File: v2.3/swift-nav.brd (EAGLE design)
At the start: 53 x 53 mm, 150 parts, among them J1 SMA_EDGE, J6 ZX62-B-5PA, Q1 IRLML6401, U1 6SLX9FTG256, U10 MAX2769, U12 PT7M8206B33TA5EX, U13 M25PX80, U2 LTC3407A_DFN, U3 STM32-M-64-LQFP, U4 7Q-16.368MBG-T, U5 SMA_PATCH_SMDGND, U6 93LC56BT-I/OT, U7 FT232HQ, U8 B4050, U9 XC2401, X3 FPGA DEBUG, X4 NX5032GA-12M, X5 CONN_5-2

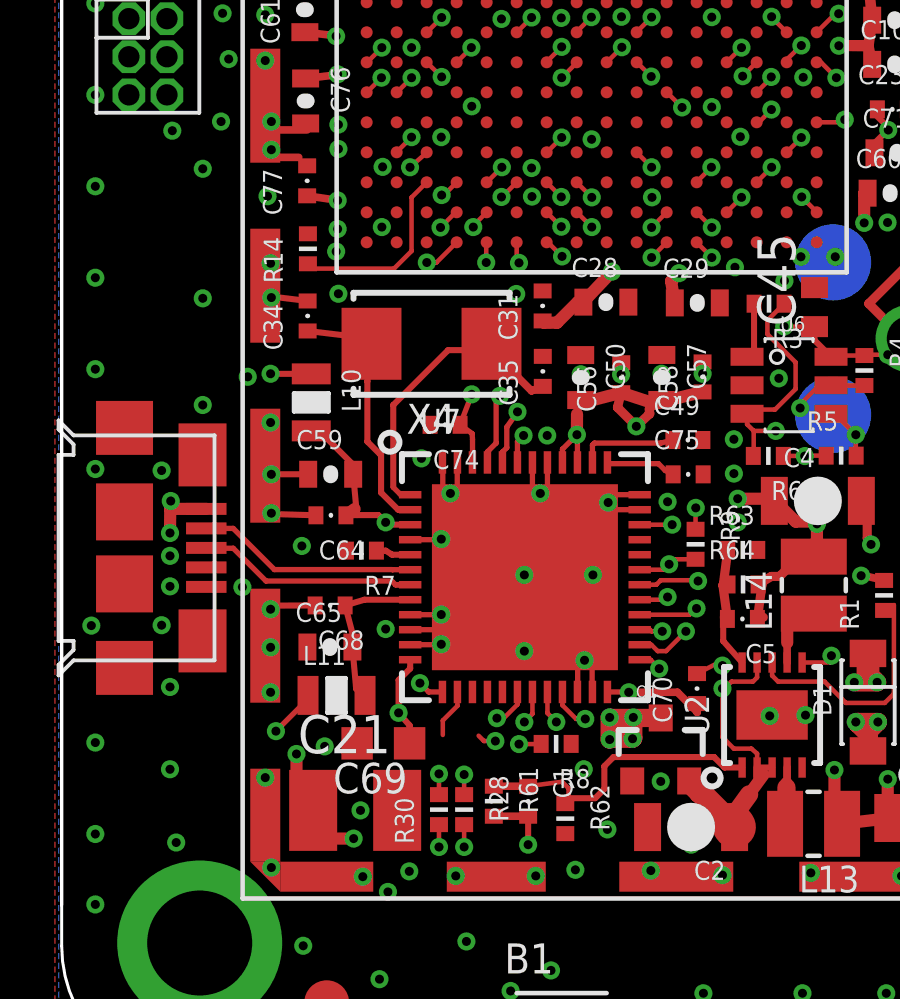
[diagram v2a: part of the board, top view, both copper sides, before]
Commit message: Routed some FTDI signals
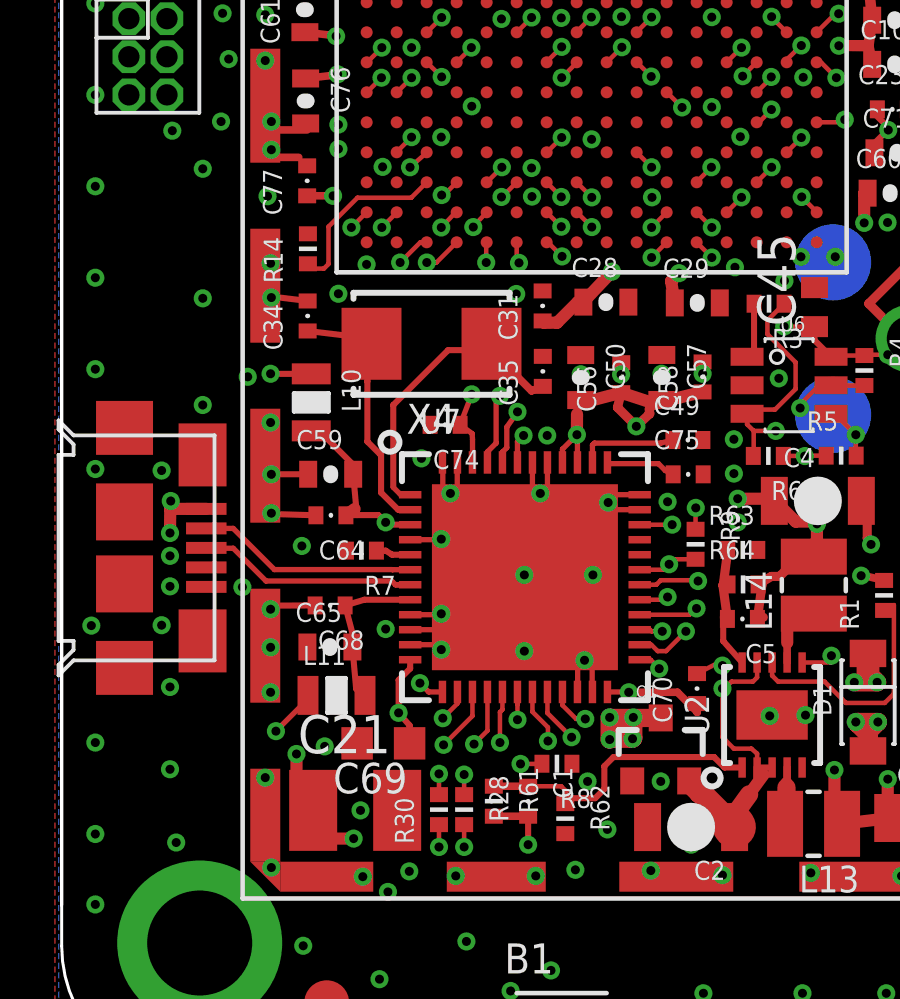
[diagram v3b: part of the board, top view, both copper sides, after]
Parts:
- moved R8 0.66 mm to (19.9, 14.0)
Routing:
- net FTDI_ADBUS2: track 0.00 -> 24.2 mm, vias 0 -> 2
- net FTDI_ADBUS3: track 0.00 -> 23.7 mm, vias 0 -> 2
- net FTDI_ADBUS4: track 0.00 -> 23.5 mm, vias 0 -> 2
- net UART6_TX/FTDI_ADBUS1: track 52.8 -> 50.7 mm
- net FTDI_ADBUS7: track 24.8 -> 26.8 mm
- net FTDI_ADBUS6: track 21.1 -> 22.8 mm
- net GND: vias 396 -> 394

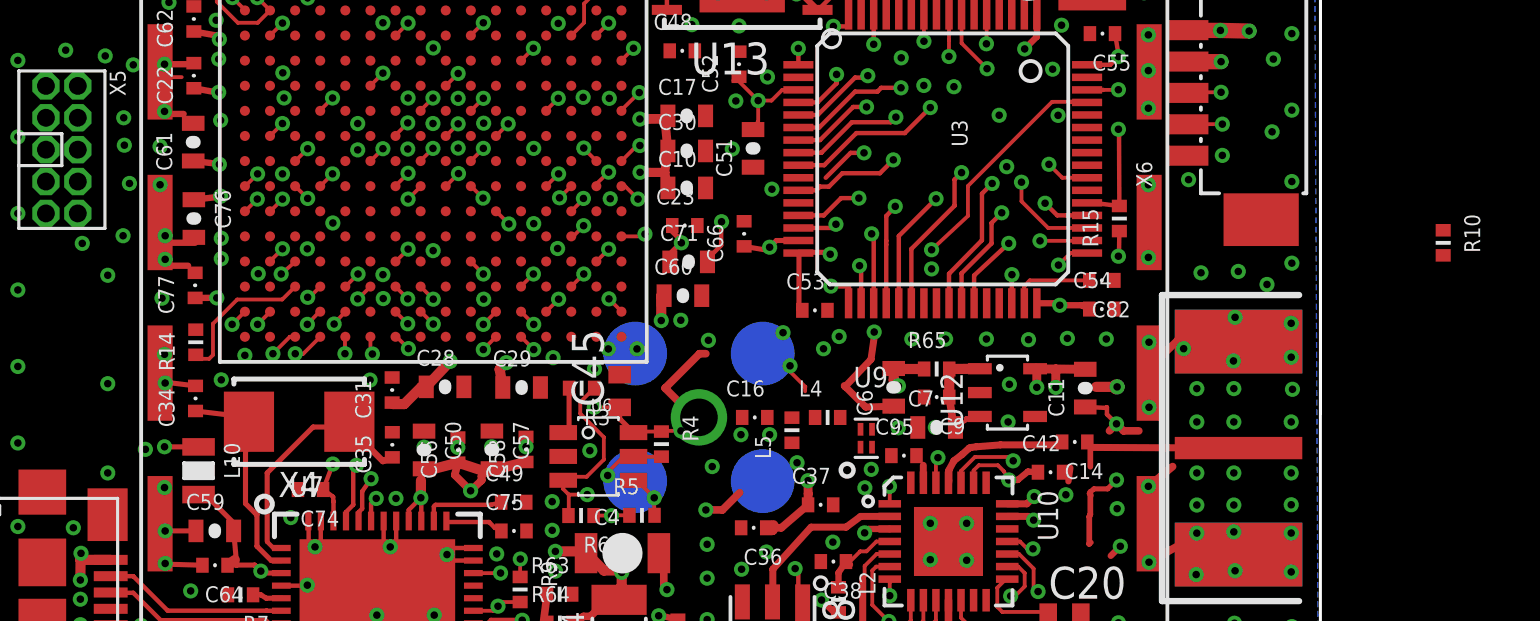
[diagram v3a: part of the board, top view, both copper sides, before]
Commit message: Routed rest of FTDI signals and added resistor to V_USB
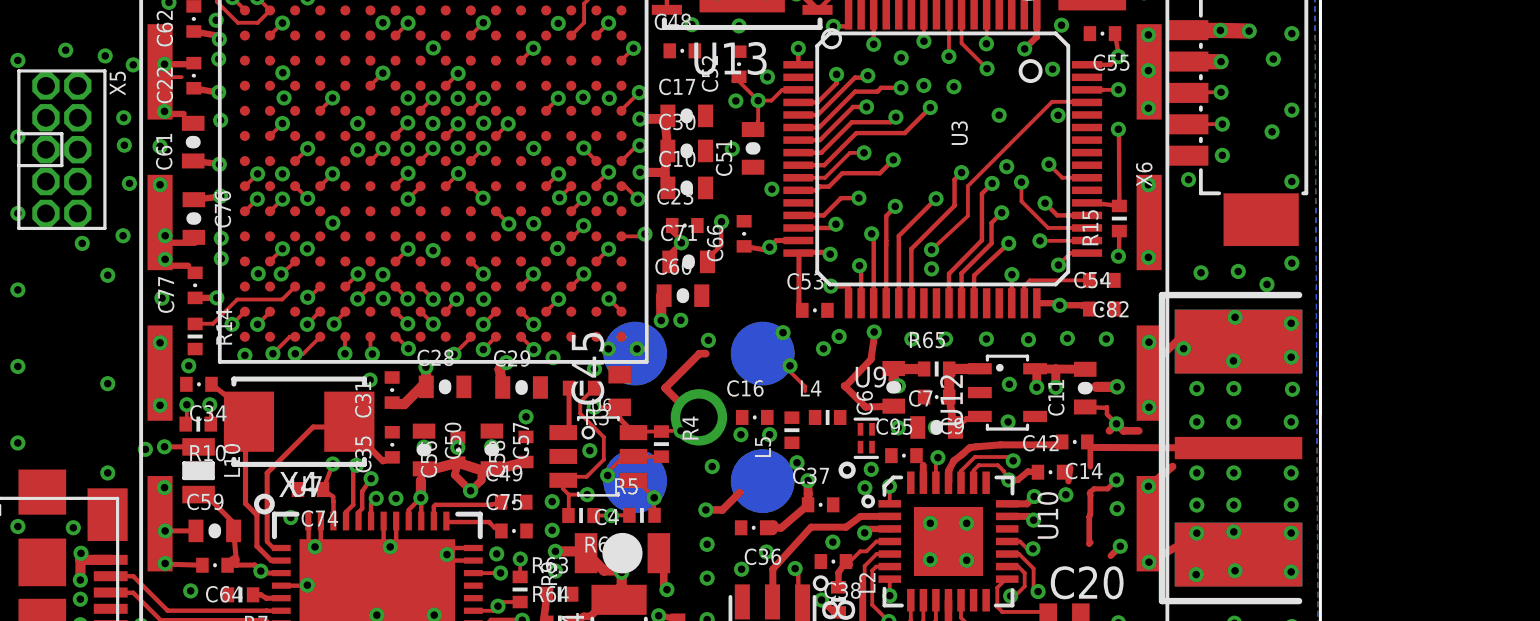
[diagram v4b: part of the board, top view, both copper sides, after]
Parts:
- moved R10 50.1 mm to (11.7, 27.9), turned to 180 degrees
- moved C34 0.58 mm to (11.7, 29.5), turned to 180 degrees
- moved R14 0.23 mm to (11.6, 31.4), turned to 270 degrees
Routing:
- net N$18: track 0.00 -> 68.0 mm, vias 0 -> 2
- net V_USB: track 131.8 -> 67.3 mm
- net UART6_TX/FTDI_ADBUS1: track 50.7 -> 52.3 mm, vias 2 -> 3
- net N$34: track 6.03 -> 4.60 mm
- net GND: track 82.6 -> 81.3 mm
- net UART6_RX/FTDI_ADBUS0: track 51.6 -> 52.7 mm, vias 2 -> 3

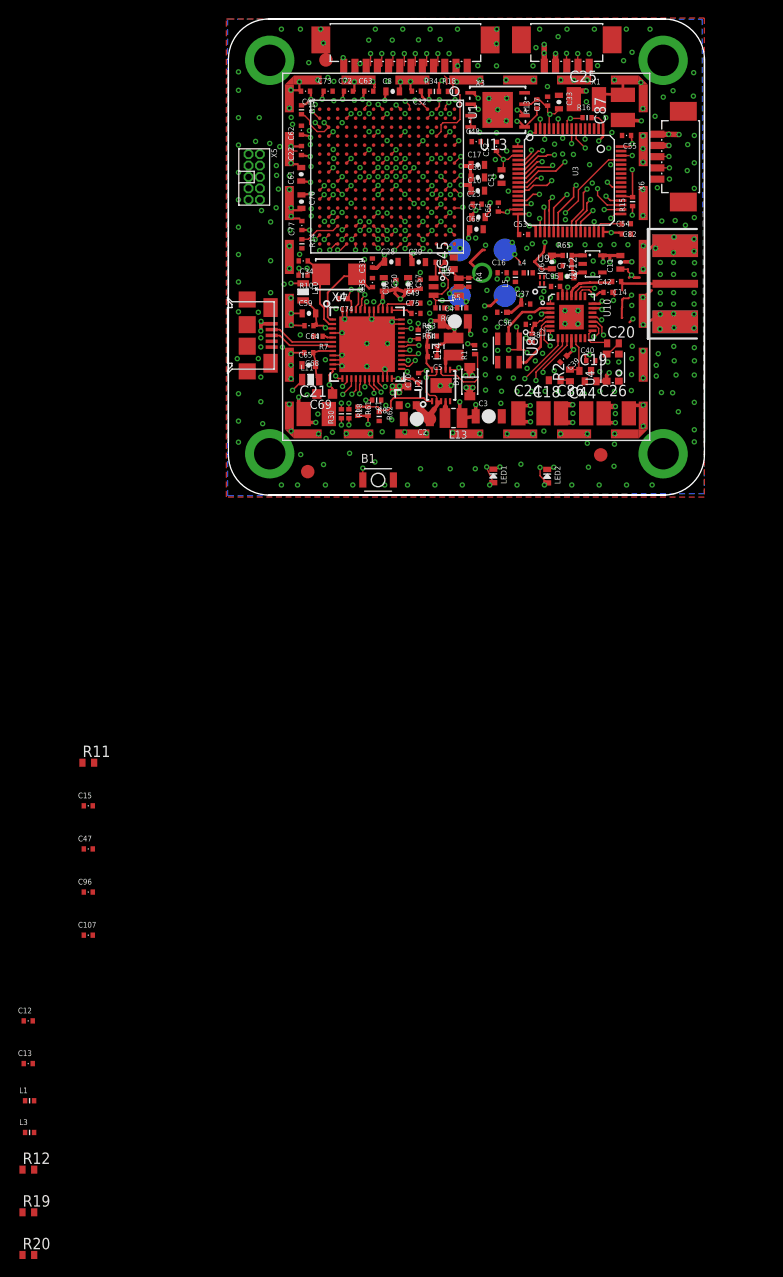
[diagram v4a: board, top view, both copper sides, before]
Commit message: Finished placing all components on board
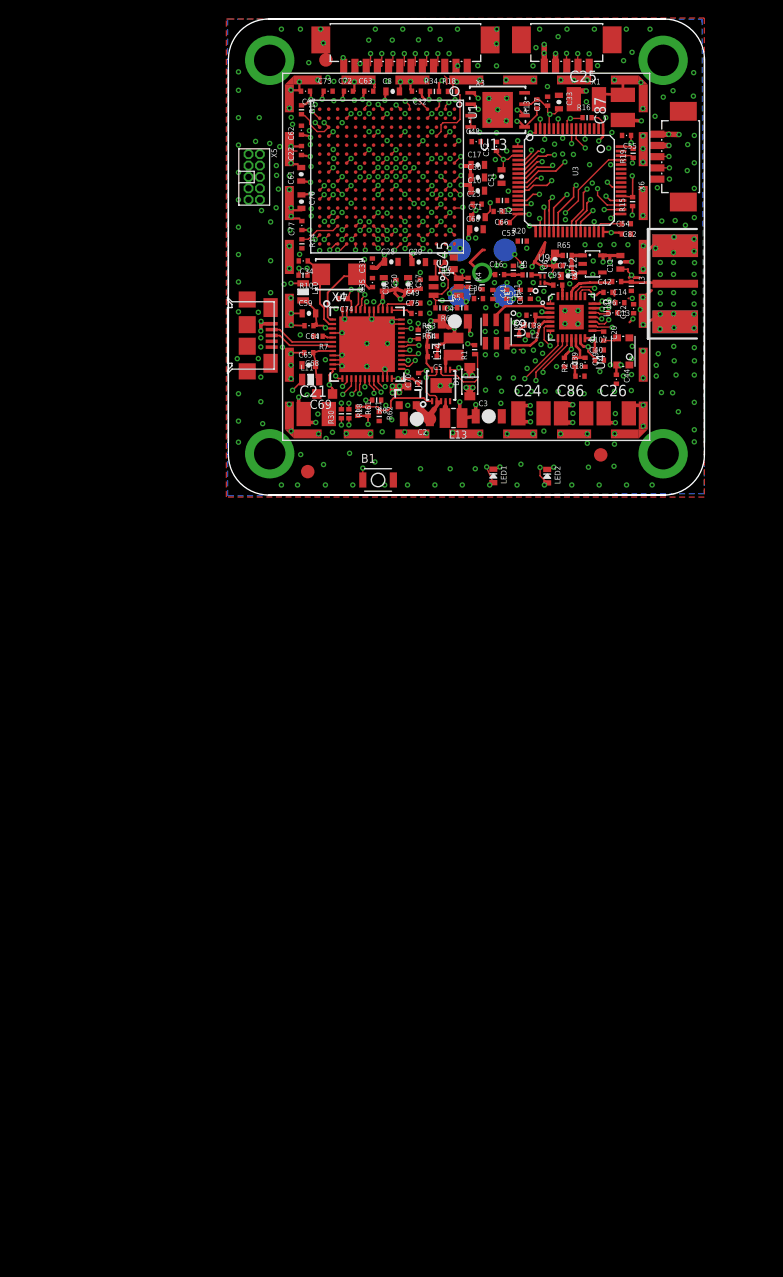
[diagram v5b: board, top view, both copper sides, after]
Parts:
- added C41: 0.47uF, pel_dipol_comp:0402-CAP
- C18, C19, C20, C44: device rcl:C0402 -> pel_dipol_comp:0402-CAP
- C36: value 0.47uF -> 100pF
- R11, R12, R19, R2, R20: device rcl:R0402 -> pel_dipol_comp:0402-RES
- moved R19 135.8 mm to (48.5, 41.5), turned to 90 degrees
- moved R20 125.6 mm to (36.1, 31.7)
- moved R12 120.1 mm to (33.9, 36.2), turned to 180 degrees
- moved L3 115.6 mm to (48.3, 26.6), turned to 270 degrees
- moved C13 107.3 mm to (47.0, 24.8), turned to 180 degrees
- moved C12 104.1 mm to (48.5, 24.1), turned to 90 degrees
- moved L1 103.9 mm to (31.6, 26.8), turned to 90 degrees
- moved C96 87.0 mm to (46.2, 23.7)
- moved C107 86.5 mm to (44.7, 19.6)
- moved C47 79.0 mm to (37.0, 25.7), turned to 90 degrees
- moved C15 74.5 mm to (35.9, 25.7), turned to 90 degrees
- moved R11 69.9 mm to (34.4, 25.8), turned to 270 degrees
- moved C37 3.46 mm to (36.3, 21.2)
- moved C36 3.01 mm to (31.2, 25.3), turned to 0 degrees
- moved C44 2.88 mm to (46.6, 16.3), turned to 270 degrees
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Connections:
- removed net N$37: C12.P$2, C13.P$2, L1.P$1, L3.P$2, U10.3
- new net N$10: C12.P$2, C13.P$2, C36.P$2, C41.P$2, L1.P$1, L3.P$2, U10.3
- net FE_CLK: now also C20.P$2; no longer C20.2
- net GND: now also C18.P$2, C19.P$2, C36.P$1, C41.P$1, C44.P$2, R20.P$1; no longer C18.2, C19.2, C36.P$2, C44.2, R20.1
- net MAX_NIDLE: now also R12.P$1; no longer R12.1
- net MAX_NSHDN: now also R19.P$1; no longer R19.1
- net MAX_PGM: now also R20.P$2; no longer R20.2
- net N$3: now also C18.P$1, R2.P$1; no longer C18.1, R2.1
- net N$4: now also C19.P$1, R2.P$2; no longer C19.1, R2.2
- net N$41: now also R11.P$1; no longer R11.1
- net N$6: now also C20.P$1; no longer C20.1
- net VCC: now also R11.P$2; no longer C36.P$1, R11.2
- net VCCIO: now also C44.P$1, R12.P$2, R19.P$2; no longer C44.1, R12.2, R19.2
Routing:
- net N$10: track 32.9 -> 29.4 mm
- net MAX_CLKOUT: track 33.4 -> 35.7 mm
- net N$6: track 3.50 -> 1.35 mm
- net N$35: track 0.00 -> 2.07 mm
- net N$14: track 0.00 -> 1.46 mm
- net MAX_Q1: track 31.0 -> 32.5 mm
- net VCCIO: track 146.7 -> 148.1 mm
- net N$4: track 4.86 -> 3.48 mm
- net VSS1: track 2.33 -> 1.02 mm
- net N$2: track 0.00 -> 1.10 mm
- net N$36: track 0.00 -> 1.01 mm
- net VDD: track 45.0 -> 45.7 mm
- net N$8: track 7.15 -> 6.41 mm
- net VCC: track 15.0 -> 14.3 mm, vias 7 -> 5
- net MAX_PGM: track 26.9 -> 26.3 mm
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
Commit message: Workin it
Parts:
- moved JP9 9.74 mm to (7.22, 45.1)
- moved C1 0.81 mm to (19.6, 12.2)
- moved R61 0.77 mm to (18.4, 12.2)
- moved R62 0.56 mm to (20.7, 12.2)
- moved R28 0.30 mm to (17.1, 12.4)
- moved C70 0.25 mm to (24.3, 16.5)
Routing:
- net GND: track 81.2 -> 79.6 mm
- net N$10: track 29.4 -> 30.4 mm
- net N$14: track 1.46 -> 2.30 mm
- net VCCIO: track 148.1 -> 148.2 mm, vias 75 -> 76

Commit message: Couple more signals to re-route
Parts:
- moved R12 3.84 mm to (35.2, 32.6)
- moved R20 1.35 mm to (35.8, 30.4), turned to 90 degrees
- moved R65 1.00 mm to (41.0, 31.1)
- moved C6 0.74 mm to (39.4, 30.3)
- moved JP9 0.69 mm to (6.54, 45.1)
- moved C7 0.50 mm to (41.0, 28.3)
- moved C11 0.46 mm to (47.0, 29.8)
- moved C9 0.46 mm to (41.0, 29.4)
- moved U12 0.46 mm to (43.9, 29.6)
- moved C13 0.06 mm to (47.0, 24.8), turned to 0 degrees
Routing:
- net JTAG_RST: track 92.5 -> 116.5 mm
- net FTDI_NRST: track 109.5 -> 103.4 mm
- net MAX_NIDLE: track 24.2 -> 29.8 mm
- net GND: track 79.6 -> 74.6 mm, vias 395 -> 406
- net MAX_PGM: track 26.3 -> 31.1 mm, vias 3 -> 4
- net VCCIO: track 148.2 -> 143.4 mm, vias 76 -> 77
- net N$41: track 0.00 -> 4.22 mm
- net N$59: track 57.4 -> 53.4 mm, vias 3 -> 4
- net N$39: track 63.5 -> 60.2 mm, vias 3 -> 4
- net V+: track 122.8 -> 119.6 mm, vias 10 -> 9
- net VDD: track 45.7 -> 43.0 mm
- net N$10: track 30.4 -> 32.5 mm
- net N$55: track 26.4 -> 28.2 mm
- net VCC: track 14.3 -> 16.0 mm, vias 5 -> 7
- net VCCINT: track 76.9 -> 75.5 mm
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
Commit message: Gettin 'er done
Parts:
- L1: value 29nH -> 29nH / DNP
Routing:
- net MAX_NSHDN: track 61.0 -> 125.7 mm, vias 2 -> 4
- net V+: track 119.6 -> 128.8 mm
- net FPGA_DONE: track 46.8 -> 51.6 mm
- net VCCIO: track 143.4 -> 140.4 mm, vias 77 -> 75
- net VCCINT: track 75.5 -> 72.6 mm, vias 16 -> 15
- net MAX_ANT_FLAG: track 93.7 -> 91.4 mm
- net FPGA_INIT_B: track 38.3 -> 40.5 mm
- net STM_CLK_IN: track 34.6 -> 35.8 mm
- net FPGA_PROGRAM_B: track 52.4 -> 51.3 mm
- net V_USB: track 66.8 -> 66.0 mm
- net FTDI_NRST: track 103.4 -> 102.7 mm
- net SPI2NSS_FLASH: track 54.3 -> 53.7 mm
- net GND: track 74.6 -> 75.1 mm, vias 406 -> 401
